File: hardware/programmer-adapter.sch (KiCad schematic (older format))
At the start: 3 parts, among them J1 Power, J2 Target, J3 Conn_ARM_JTAG_SWD_20

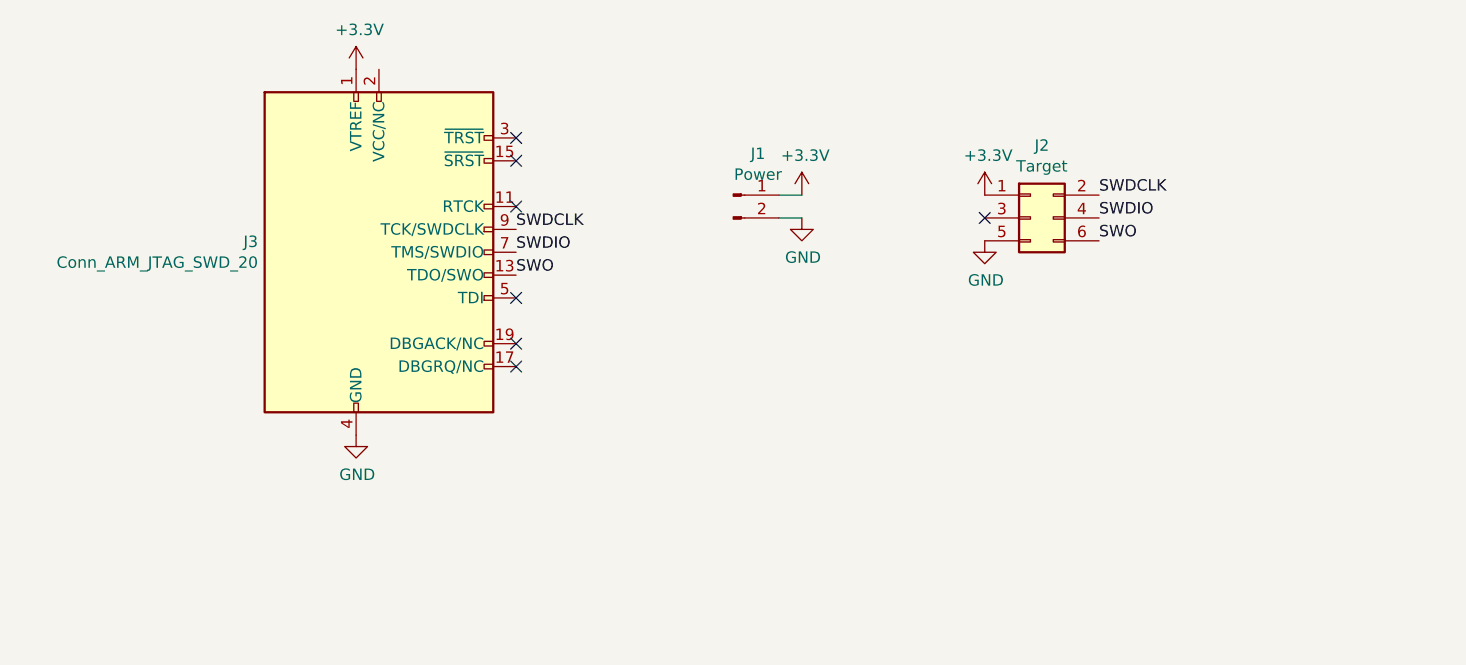
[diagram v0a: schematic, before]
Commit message: Added power designators
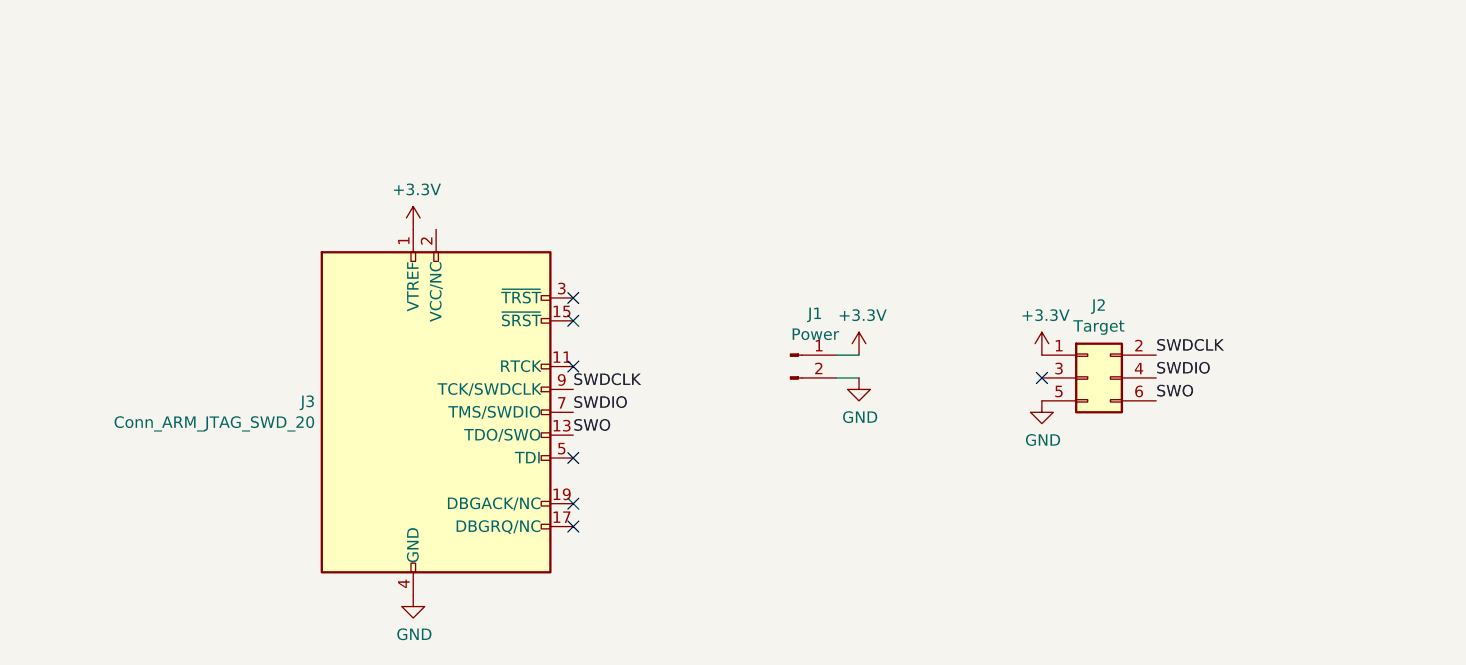
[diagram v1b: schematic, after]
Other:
- moved on the sheet: J1, J2, J3
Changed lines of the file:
@@
 encoding utf-8
 Sheet 1 1
-Title "Device template"
-Date ""
-Rev ""
+Title "Programmer adapter"
+Date "2020-02-22"
+Rev "1.0.1"
 Comp "Chameleon Electronics "
 Comment1 ""
@@
 L Connector:Conn_ARM_JTAG_SWD_20 J3
 U 1 1 5E4FBF88
-P 4150 3450
-F 0 "J3" H 3621 3496 50  0000 R CNN
-F 1 "Conn_ARM_JTAG_SWD_20" H 3621 3405 50  0000 R CNN
-F 2 "Connector_PinSocket_2.54mm:PinSocket_2x10_P2.54mm_Horizontal" H 4600 2400 50  0001 L TNN
-F 3 "http://infocenter.arm.com/help/topic/com.arm.doc.dui0499b/DUI0499B_system_design_reference.pdf" V 3800 2200 50  0001 C CNN
-	1    4150 3450
+P 4400 4150
+F 0 "J3" H 3871 4196 50  0000 R CNN
+F 1 "Conn_ARM_JTAG_SWD_20" H 3871 4105 50  0000 R CNN
+F 2 "Connector_PinSocket_2.54mm:PinSocket_2x10_P2.54mm_Horizontal" H 4850 3100 50  0001 L TNN
+F 3 "http://infocenter.arm.com/help/topic/com.arm.doc.dui0499b/DUI0499B_system_design_reference.pdf" V 4050 2900 50  0001 C CNN
+	1    4400 4150
 	1    0    0    -1
 $EndComp
-Text Label 4750 3450 0    50   ~ 0
+Text Label 5000 4150 0    50   ~ 0
 SWDIO
-Text Label 4750 3350 0    50   ~ 0
+Text Label 5000 4050 0    50   ~ 0
 SWDCLK
-Text Label 4750 3550 0    50   ~ 0
+Text Label 5000 4250 0    50   ~ 0
 SWO
 $Comp
 L power:GND #PWR06
 U 1 1 5E4FCD55
-P 4050 4250
-F 0 "#PWR06" H 4050 4000 50  0001 C CNN
-F 1 "GND" H 4055 4077 50  0000 C CNN
-F 2 "" H 4050 4250 50  0001 C CNN
-F 3 "" H 4050 4250 50  0001 C CNN
-	1    4050 4250
+P 4300 4950
+F 0 "#PWR06" H 4300 4700 50  0001 C CNN
+F 1 "GND" H 4305 4777 50  0000 C CNN
+F 2 "" H 4300 4950 50  0001 C CNN
+F 3 "" H 4300 4950 50  0001 C CNN
+	1    4300 4950
 	1    0    0    -1
 $EndComp
-NoConn ~ 4750 2950
-NoConn ~ 4750 3050
-NoConn ~ 4750 3250
-NoConn ~ 4750 3650
-NoConn ~ 4750 3850
-NoConn ~ 4750 3950
+NoConn ~ 5000 3650
+NoConn ~ 5000 3750
+NoConn ~ 5000 3950
+NoConn ~ 5000 4350
+NoConn ~ 5000 4550
+NoConn ~ 5000 4650
 $Comp
 L power:+3.3V #PWR01
 U 1 1 5E4FE2E4
-P 4050 2650
-F 0 "#PWR01" H 4050 2500 50  0001 C CNN
-F 1 "+3.3V" H 4065 2823 50  0000 C CNN
-F 2 "" H 4050 2650 50  0001 C CNN
-F 3 "" H 4050 2650 50  0001 C CNN
-	1    4050 2650
+P 4300 3350
+F 0 "#PWR01" H 4300 3200 50  0001 C CNN
+F 1 "+3.3V" H 4315 3523 50  0000 C CNN
+F 2 "" H 4300 3350 50  0001 C CNN
+F 3 "" H 4300 3350 50  0001 C CNN
+	1    4300 3350
 	1    0    0    -1
 $EndComp
@@
 L Connector:Conn_01x02_Male J1
 U 1 1 5E4FF8ED
-P 5700 3200
-F 0 "J1" H 5808 3381 50  0000 C CNN
-F 1 "Power" H 5808 3290 50  0000 C CNN
-F 2 "Connector_PinHeader_2.54mm:PinHeader_1x02_P2.54mm_Vertical" H 5700 3200 50  0001 C CNN
-F 3 "~" H 5700 3200 50  0001 C CNN
-	1    5700 3200
+P 5950 3900
+F 0 "J1" H 6058 4081 50  0000 C CNN
+F 1 "Power" H 6058 3990 50  0000 C CNN
+F 2 "Connector_PinHeader_2.54mm:PinHeader_1x02_P2.54mm_Vertical" H 5950 3900 50  0001 C CNN
+F 3 "~" H 5950 3900 50  0001 C CNN
+	1    5950 3900
 	1    0    0    -1
 $EndComp
@@
 L power:+3.3V #PWR02
 U 1 1 5E500A0C
-P 6000 3200
-F 0 "#PWR02" H 6000 3050 50  0001 C CNN
-F 1 "+3.3V" H 6015 3373 50  0000 C CNN
-F 2 "" H 6000 3200 50  0001 C CNN
-F 3 "" H 6000 3200 50  0001 C CNN
-	1    6000 3200
+P 6250 3900
+F 0 "#PWR02" H 6250 3750 50  0001 C CNN
+F 1 "+3.3V" H 6265 4073 50  0000 C CNN
+F 2 "" H 6250 3900 50  0001 C CNN
+F 3 "" H 6250 3900 50  0001 C CNN
+	1    6250 3900
 	1    0    0    -1
 $EndComp
 Wire Wire Line
-	6000 3200 5900 3200
+	6250 3900 6150 3900
 $Comp
 L power:GND #PWR04
 U 1 1 5E500F8E
-P 6000 3300
-F 0 "#PWR04" H 6000 3050 50  0001 C CNN
-F 1 "GND" H 6005 3127 50  0000 C CNN
-F 2 "" H 6000 3300 50  0001 C CNN
-F 3 "" H 6000 3300 50  0001 C CNN
-	1    6000 3300
+P 6250 4000
+F 0 "#PWR04" H 6250 3750 50  0001 C CNN
+F 1 "GND" H 6255 3827 50  0000 C CNN
+F 2 "" H 6250 4000 50  0001 C CNN
+F 3 "" H 6250 4000 50  0001 C CNN
+	1    6250 4000
 	1    0    0    -1
 $EndComp
 Wire Wire Line
-	6000 3300 5900 3300
+	6250 4000 6150 4000
 $Comp
 L Connector_Generic:Conn_02x03_Odd_Even J2
 U 1 1 5E501B04
-P 7000 3300
-F 0 "J2" H 7050 3617 50  0000 C CNN
-F 1 "Target" H 7050 3526 50  0000 C CNN
-F 2 "Connector_PinHeader_1.27mm:PinHeader_2x03_P1.27mm_Vertical_SMD" H 7000 3300 50  0001 C CNN
-F 3 "~" H 7000 3300 50  0001 C CNN
-	1    7000 3300
+P 7250 4000
+F 0 "J2" H 7300 4317 50  0000 C CNN
+F 1 "Target" H 7300 4226 50  0000 C CNN
+F 2 "Connector_PinHeader_1.27mm:PinHeader_2x03_P1.27mm_Vertical_SMD" H 7250 4000 50  0001 C CNN
+F 3 "~" H 7250 4000 50  0001 C CNN
+	1    7250 4000
 	1    0    0    -1
 $EndComp
@@
 L power:+3.3V #PWR03
 U 1 1 5E508EC0
-P 6800 3200
-F 0 "#PWR03" H 6800 3050 50  0001 C CNN
-F 1 "+3.3V" H 6815 3373 50  0000 C CNN
-F 2 "" H 6800 3200 50  0001 C CNN
-F 3 "" H 6800 3200 50  0001 C CNN
-	1    6800 3200
+P 7050 3900
+F 0 "#PWR03" H 7050 3750 50  0001 C CNN
+F 1 "+3.3V" H 7065 4073 50  0000 C CNN
+F 2 "" H 7050 3900 50  0001 C CNN
+F 3 "" H 7050 3900 50  0001 C CNN
+	1    7050 3900
 	1    0    0    -1
 $EndComp
@@
 L power:GND #PWR05
 U 1 1 5E5092F6
-P 6800 3400
-F 0 "#PWR05" H 6800 3150 50  0001 C CNN
-F 1 "GND" H 6805 3227 50  0000 C CNN
-F 2 "" H 6800 3400 50  0001 C CNN
-F 3 "" H 6800 3400 50  0001 C CNN
-	1    6800 3400
+P 7050 4100
+F 0 "#PWR05" H 7050 3850 50  0001 C CNN
+F 1 "GND" H 7055 3927 50  0000 C CNN
+F 2 "" H 7050 4100 50  0001 C CNN
+F 3 "" H 7050 4100 50  0001 C CNN
+	1    7050 4100
 	1    0    0    -1
 $EndComp
-Text Label 7300 3300 0    50   ~ 0
+Text Label 7550 4000 0    50   ~ 0
 SWDIO
-Text Label 7300 3200 0    50   ~ 0
+Text Label 7550 3900 0    50   ~ 0
 SWDCLK
-Text Label 7300 3400 0    50   ~ 0
+Text Label 7550 4100 0    50   ~ 0
 SWO
-NoConn ~ 6800 3300
+NoConn ~ 7050 4000
 $EndSCHEMATC

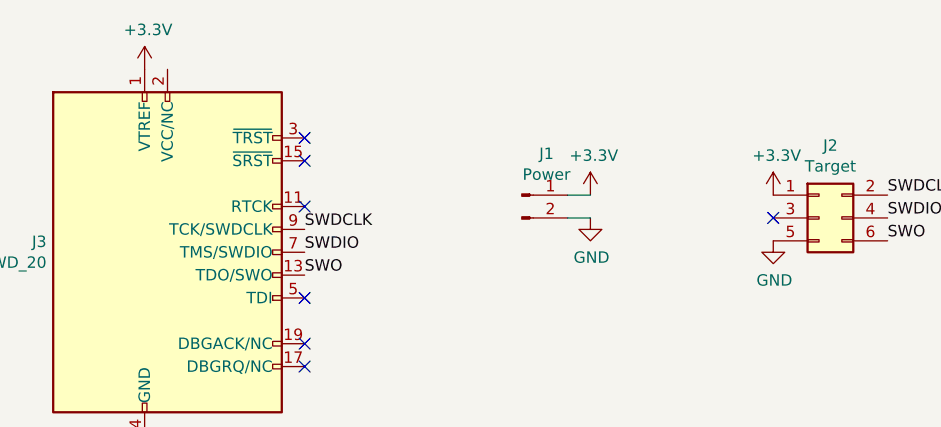
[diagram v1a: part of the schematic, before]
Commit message: Added reset signal
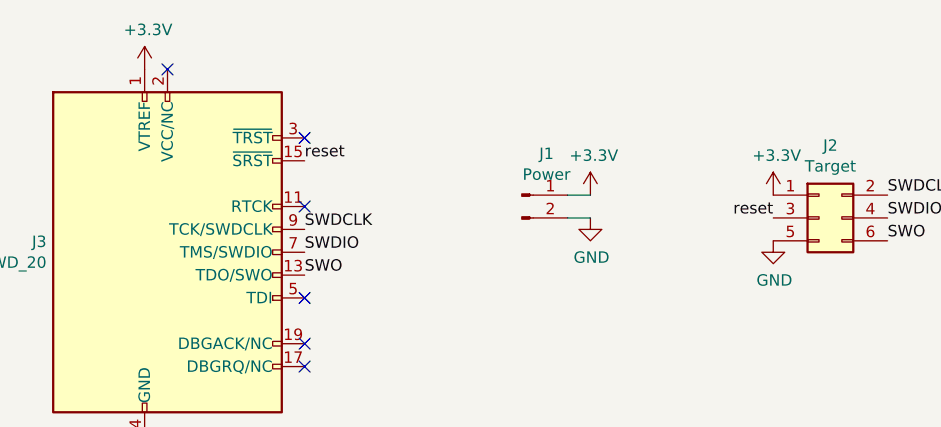
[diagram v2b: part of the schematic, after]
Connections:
- net reset: now reaches J3.15 (~SRST~)
- net reset: now also J2.3 (Pin_3)
- no-connect marks 7 -> 6
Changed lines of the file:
@@
 Sheet 1 1
 Title "Programmer adapter"
-Date "2020-02-22"
-Rev "1.0.1"
+Date "2020-03-09"
+Rev "1.1.0"
 Comp "Chameleon Electronics "
 Comment1 ""
@@
 $EndComp
 NoConn ~ 5000 3650
-NoConn ~ 5000 3750
 NoConn ~ 5000 3950
 NoConn ~ 5000 4350
@@
 Text Label 7550 4100 0    50   ~ 0
 SWO
-NoConn ~ 7050 4000
+Text Label 5000 3750 0    50   ~ 0
+reset
+Text Label 7050 4000 2    50   ~ 0
+reset
+NoConn ~ 4400 3350
 $EndSCHEMATC

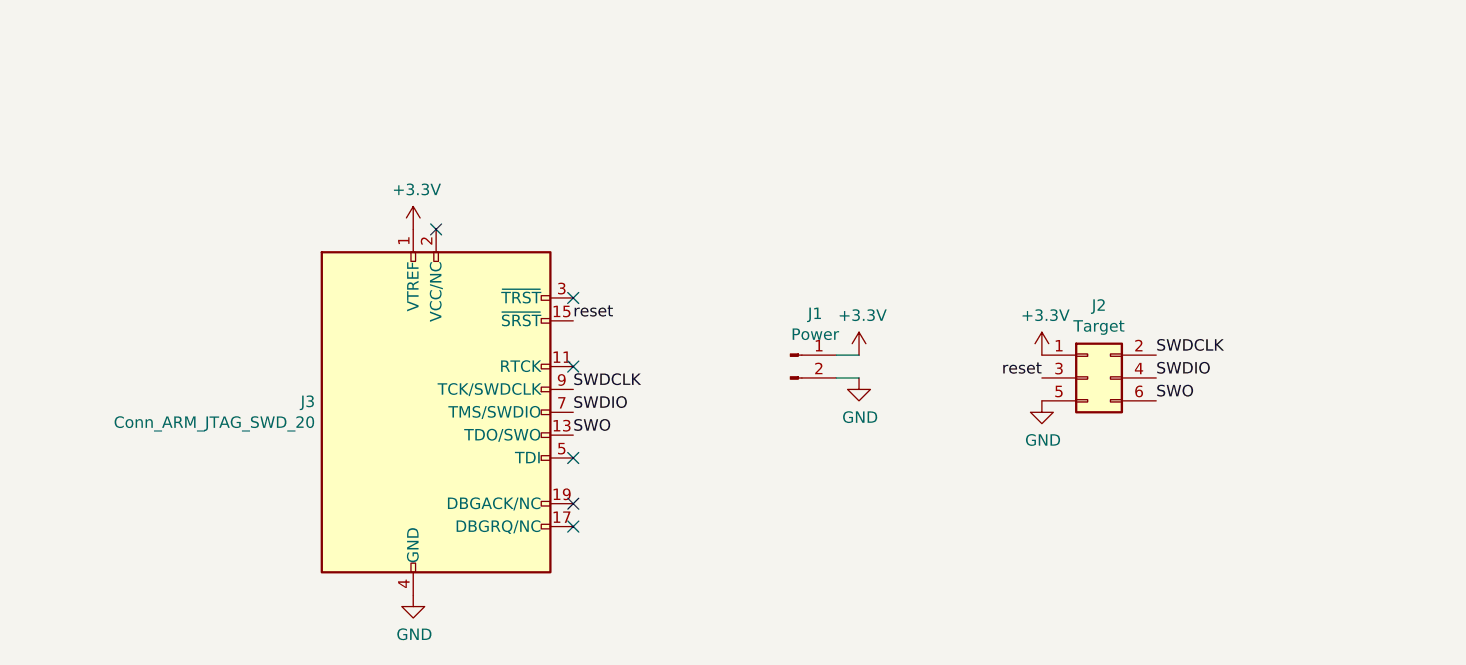
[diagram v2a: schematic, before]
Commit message: Voltage Regulator Supply
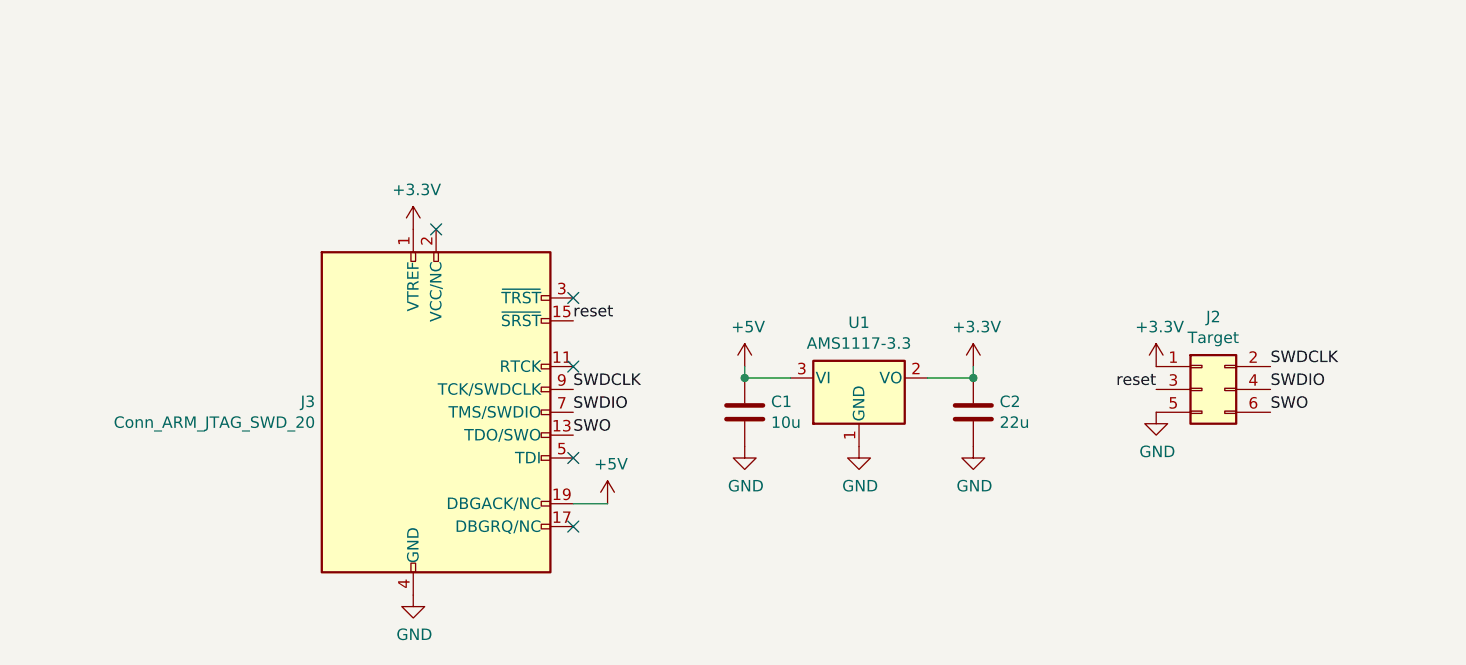
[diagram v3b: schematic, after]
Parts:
- removed J1: Power, Connector_PinHeader_2.54mm:PinHeader_1x02_P2.54mm_Vertical, symbol Connector:Conn_01x02_Male
- added C1: 10u, Capacitor_SMD:C_0805_2012Metric, symbol Device:C
- added C2: 22u, Capacitor_SMD:C_0805_2012Metric, symbol Device:C
- added U1: AMS1117-3.3, Package_TO_SOT_SMD:SOT-223-3_TabPin2, symbol Regulator_Linear:AMS1117-3.3
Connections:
- net +3V3: now also C2.1, U1.2 (VO)
- net GND: now also C1.2, C2.2, U1.1 (GND)
- net +5V: now reaches J3.19 (DBGACK/NC)
- net +5V: now also C1.1, U1.3 (VI)
- no-connect marks 6 -> 5
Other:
- moved on the sheet: J2
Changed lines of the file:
@@
 NoConn ~ 5000 3950
 NoConn ~ 5000 4350
-NoConn ~ 5000 4550
 NoConn ~ 5000 4650
 $Comp
@@
 $EndComp
 $Comp
-L Connector:Conn_01x02_Male J1
-U 1 1 5E4FF8ED
-P 5950 3900
-F 0 "J1" H 6058 4081 50  0000 C CNN
-F 1 "Power" H 6058 3990 50  0000 C CNN
-F 2 "Connector_PinHeader_2.54mm:PinHeader_1x02_P2.54mm_Vertical" H 5950 3900 50  0001 C CNN
-F 3 "~" H 5950 3900 50  0001 C CNN
-	1    5950 3900
-	1    0    0    -1
-$EndComp
-$Comp
-L power:+3.3V #PWR02
-U 1 1 5E500A0C
-P 6250 3900
-F 0 "#PWR02" H 6250 3750 50  0001 C CNN
-F 1 "+3.3V" H 6265 4073 50  0000 C CNN
-F 2 "" H 6250 3900 50  0001 C CNN
-F 3 "" H 6250 3900 50  0001 C CNN
-	1    6250 3900
-	1    0    0    -1
-$EndComp
-Wire Wire Line
-	6250 3900 6150 3900
-$Comp
-L power:GND #PWR04
-U 1 1 5E500F8E
-P 6250 4000
-F 0 "#PWR04" H 6250 3750 50  0001 C CNN
-F 1 "GND" H 6255 3827 50  0000 C CNN
-F 2 "" H 6250 4000 50  0001 C CNN
-F 3 "" H 6250 4000 50  0001 C CNN
-	1    6250 4000
-	1    0    0    -1
-$EndComp
-Wire Wire Line
-	6250 4000 6150 4000
-$Comp
 L Connector_Generic:Conn_02x03_Odd_Even J2
 U 1 1 5E501B04
-P 7250 4000
-F 0 "J2" H 7300 4317 50  0000 C CNN
-F 1 "Target" H 7300 4226 50  0000 C CNN
-F 2 "Connector_PinHeader_1.27mm:PinHeader_2x03_P1.27mm_Vertical_SMD" H 7250 4000 50  0001 C CNN
-F 3 "~" H 7250 4000 50  0001 C CNN
-	1    7250 4000
+P 7750 4050
+F 0 "J2" H 7800 4367 50  0000 C CNN
+F 1 "Target" H 7800 4276 50  0000 C CNN
+F 2 "Connector_PinHeader_1.27mm:PinHeader_2x03_P1.27mm_Vertical_SMD" H 7750 4050 50  0001 C CNN
+F 3 "~" H 7750 4050 50  0001 C CNN
+	1    7750 4050
 	1    0    0    -1
 $EndComp
@@
 L power:+3.3V #PWR03
 U 1 1 5E508EC0
-P 7050 3900
-F 0 "#PWR03" H 7050 3750 50  0001 C CNN
-F 1 "+3.3V" H 7065 4073 50  0000 C CNN
-F 2 "" H 7050 3900 50  0001 C CNN
-F 3 "" H 7050 3900 50  0001 C CNN
-	1    7050 3900
+P 7550 3950
+F 0 "#PWR03" H 7550 3800 50  0001 C CNN
+F 1 "+3.3V" H 7565 4123 50  0000 C CNN
+F 2 "" H 7550 3950 50  0001 C CNN
+F 3 "" H 7550 3950 50  0001 C CNN
+	1    7550 3950
 	1    0    0    -1
 $EndComp
@@
 L power:GND #PWR05
 U 1 1 5E5092F6
-P 7050 4100
-F 0 "#PWR05" H 7050 3850 50  0001 C CNN
-F 1 "GND" H 7055 3927 50  0000 C CNN
-F 2 "" H 7050 4100 50  0001 C CNN
-F 3 "" H 7050 4100 50  0001 C CNN
-	1    7050 4100
+P 7550 4150
+F 0 "#PWR05" H 7550 3900 50  0001 C CNN
+F 1 "GND" H 7555 3977 50  0000 C CNN
+F 2 "" H 7550 4150 50  0001 C CNN
+F 3 "" H 7550 4150 50  0001 C CNN
+	1    7550 4150
 	1    0    0    -1
 $EndComp
-Text Label 7550 4000 0    50   ~ 0
+Text Label 8050 4050 0    50   ~ 0
 SWDIO
-Text Label 7550 3900 0    50   ~ 0
+Text Label 8050 3950 0    50   ~ 0
 SWDCLK
-Text Label 7550 4100 0    50   ~ 0
+Text Label 8050 4150 0    50   ~ 0
 SWO
 Text Label 5000 3750 0    50   ~ 0
 reset
-Text Label 7050 4000 2    50   ~ 0
+Text Label 7550 4050 2    50   ~ 0
 reset
+$Comp
+L Regulator_Linear:AMS1117-3.3 U1
+U 1 1 5ED5B523
+P 6250 4000
+F 0 "U1" H 6250 4242 50  0000 C CNN
+F 1 "AMS1117-3.3" H 6250 4151 50  0000 C CNN
+F 2 "Package_TO_SOT_SMD:SOT-223-3_TabPin2" H 6250 4200 50  0001 C CNN
+F 3 "http://www.advanced-monolithic.com/pdf/ds1117.pdf" H 6350 3750 50  0001 C CNN
+	1    6250 4000
+	1    0    0    -1
+$EndComp
+$Comp
+L power:+5V #PWR0101
+U 1 1 5ED5BE1C
+P 5150 4550
+F 0 "#PWR0101" H 5150 4400 50  0001 C CNN
+F 1 "+5V" H 5165 4723 50  0000 C CNN
+F 2 "" H 5150 4550 50  0001 C CNN
+F 3 "" H 5150 4550 50  0001 C CNN
+	1    5150 4550
+	1    0    0    -1
+$EndComp
+$Comp
+L power:+5V #PWR0102
+U 1 1 5ED5E701
+P 5750 3950
+F 0 "#PWR0102" H 5750 3800 50  0001 C CNN
+F 1 "+5V" H 5765 4123 50  0000 C CNN
+F 2 "" H 5750 3950 50  0001 C CNN
+F 3 "" H 5750 3950 50  0001 C CNN
+	1    5750 3950
+	1    0    0    -1
+$EndComp
+Wire Wire Line
+	5750 3950 5750 4000
+Wire Wire Line
+	5750 4000 5950 4000
+$Comp
+L power:GND #PWR0103
+U 1 1 5ED5EF4A
+P 6250 4300
+F 0 "#PWR0103" H 6250 4050 50  0001 C CNN
+F 1 "GND" H 6255 4127 50  0000 C CNN
+F 2 "" H 6250 4300 50  0001 C CNN
+F 3 "" H 6250 4300 50  0001 C CNN
+	1    6250 4300
+	1    0    0    -1
+$EndComp
+$Comp
+L power:+3.3V #PWR0104
+U 1 1 5ED5F3AA
+P 6750 3950
+F 0 "#PWR0104" H 6750 3800 50  0001 C CNN
+F 1 "+3.3V" H 6765 4123 50  0000 C CNN
+F 2 "" H 6750 3950 50  0001 C CNN
+F 3 "" H 6750 3950 50  0001 C CNN
+	1    6750 3950
+	1    0    0    -1
+$EndComp
+Wire Wire Line
+	6750 3950 6750 4000
+Wire Wire Line
+	6750 4000 6550 4000
+$Comp
+L Device:C C1
+U 1 1 5ED6736D
+P 5750 4150
+F 0 "C1" H 5865 4196 50  0000 L CNN
+F 1 "10u" H 5865 4105 50  0000 L CNN
+F 2 "Capacitor_SMD:C_0805_2012Metric" H 5788 4000 50  0001 C CNN
+F 3 "~" H 5750 4150 50  0001 C CNN
+	1    5750 4150
+	1    0    0    -1
+$EndComp
+Connection ~ 5750 4000
+$Comp
+L Device:C C2
+U 1 1 5ED697B9
+P 6750 4150
+F 0 "C2" H 6865 4196 50  0000 L CNN
+F 1 "22u" H 6865 4105 50  0000 L CNN
+F 2 "Capacitor_SMD:C_0805_2012Metric" H 6788 4000 50  0001 C CNN
+F 3 "~" H 6750 4150 50  0001 C CNN
+	1    6750 4150
+	1    0    0    -1
+$EndComp
+Connection ~ 6750 4000
+$Comp
+L power:GND #PWR0105
+U 1 1 5ED69C3E
+P 5750 4300
+F 0 "#PWR0105" H 5750 4050 50  0001 C CNN
+F 1 "GND" H 5755 4127 50  0000 C CNN
+F 2 "" H 5750 4300 50  0001 C CNN
+F 3 "" H 5750 4300 50  0001 C CNN
+	1    5750 4300
+	1    0    0    -1
+$EndComp
+$Comp
+L power:GND #PWR0106
+U 1 1 5ED69F09
+P 6750 4300
+F 0 "#PWR0106" H 6750 4050 50  0001 C CNN
+F 1 "GND" H 6755 4127 50  0000 C CNN
+F 2 "" H 6750 4300 50  0001 C CNN
+F 3 "" H 6750 4300 50  0001 C CNN
+	1    6750 4300
+	1    0    0    -1
+$EndComp
+Wire Wire Line
+	5150 4550 5000 4550
 NoConn ~ 4400 3350
 $EndSCHEMATC
